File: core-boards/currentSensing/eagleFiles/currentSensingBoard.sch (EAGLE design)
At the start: 22 parts, among them Q1 16MHz, X2 2-PIN_2MM-H, X3 4-PIN_2MM-H

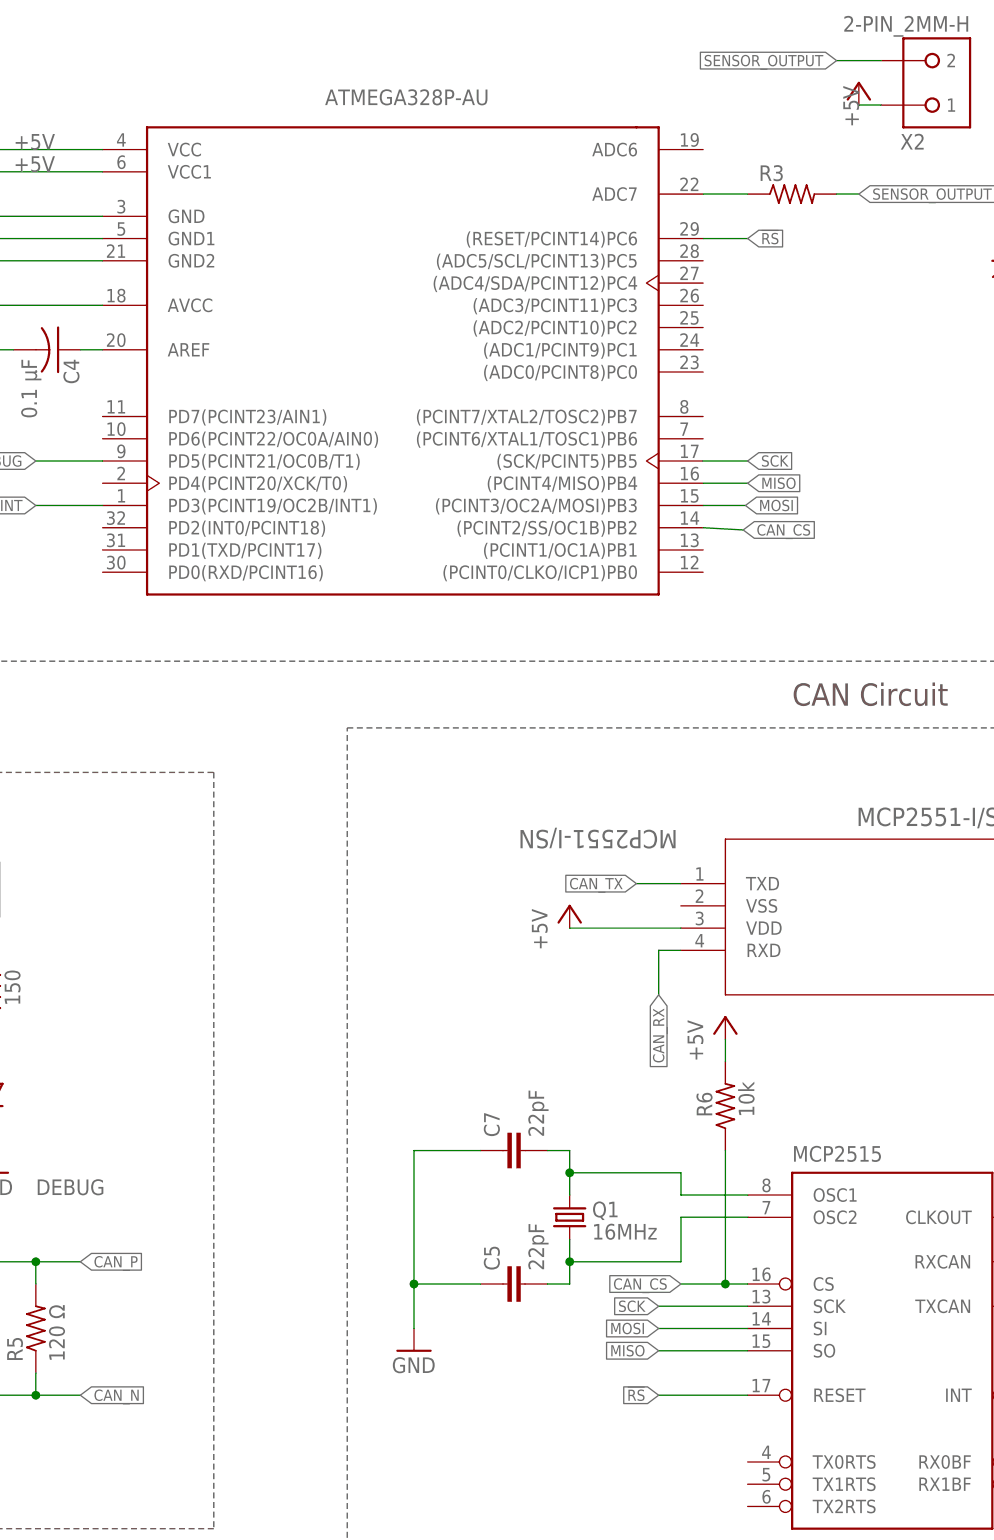
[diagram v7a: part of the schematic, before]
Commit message: Updated Oscillator
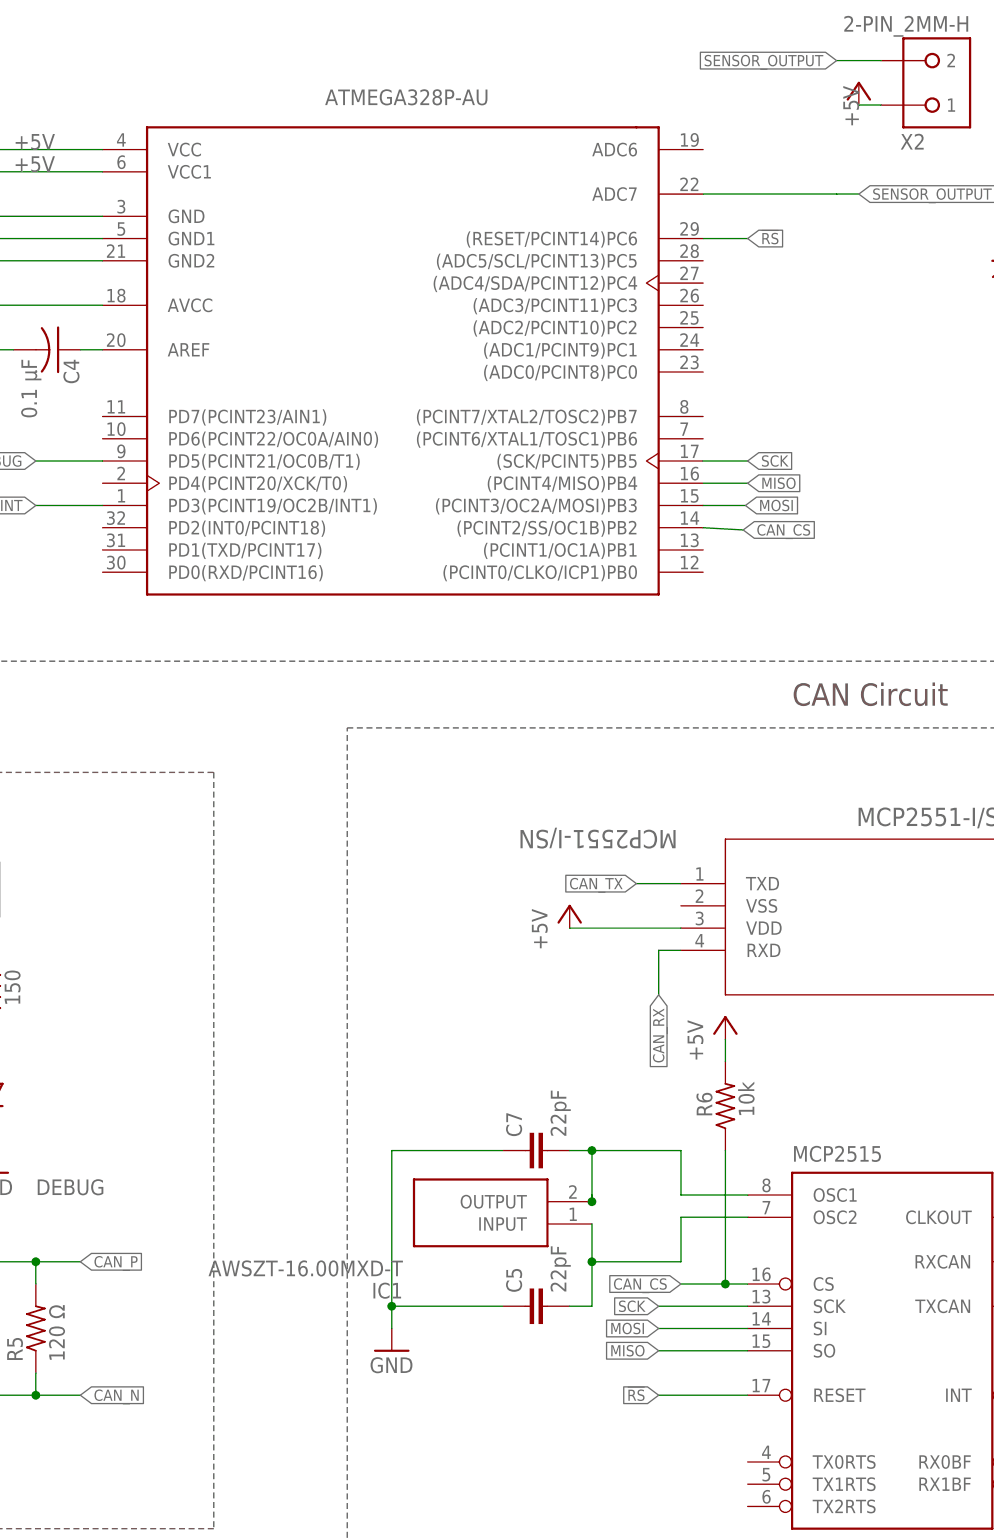
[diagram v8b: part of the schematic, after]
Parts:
- removed Q1: 16MHz, SparkFun-FreqCtrl:CRYSTAL5X3
- removed R3: (no value), RoboJackets-Resistors:R0603W
- added IC1: AWSZT-16.00MXD-T, AWSZT-16.00MXD-T:AWSZT-16.00MXD-T
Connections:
- removed net N$17: C7.2, MCP2515>NAME.OSC1, Q1.2
- removed net N$18: C5.2, MCP2515>NAME.OSC2, Q1.1
- removed net N$2: ATMEGA328P-AU(V1).ADC7, R3.PIN1
- new net CLK1: C5.2, IC1.INPUT, MCP2515>NAME.OSC2
- new net CLK2: C7.2, IC1.OUTPUT, MCP2515>NAME.OSC1
- net SENSOR_OUTPUT: now also ATMEGA328P-AU(V1).ADC7; no longer R3.PIN2
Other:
- moved on the sheet: C5, C7
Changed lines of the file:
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@@
 <?xml version="1.0" encoding="utf-8"?>
 <!DOCTYPE eagle SYSTEM "eagle.dtd">
-<eagle version="9.5.2">
+<eagle version="9.6.2">
 <drawing>
 <settings>
@@
 <part name="C6" library="rcl" library_urn="urn:adsk.eagle:library:334" deviceset="C-US" device="C0603" package3d_urn="urn:adsk.eagle:package:23616/2" value="0.1 µF"/>
 <part name="MCP2515" library="SparkFun-DigitalIC" deviceset="MCP2510" device="SO" value="MCP2515"/>
-<part name="Q1" library="SparkFun-FreqCtrl" deviceset="CRYSTAL" device="5X3" value="16MHz"/>
 <part name="C5" library="SparkFun-Capacitors" deviceset="22PF-50V-5%(0603)" device="" value="22pF"/>
 <part name="C7" library="SparkFun-Capacitors" deviceset="22PF-50V-5%(0603)" device="" value="22pF"/>
@@
 <part name="DEBUG" library="RoboJackets-LEDs" deviceset="LED-SMD" device="" technology="-RED" value="RED"/>
 <part name="FRAME1" library="RoboJackets-Frames" deviceset="FRAME_B_L" device=""/>
-<part name="R3" library="RoboJackets-Resistors" deviceset="R0603W" device=""/>
+<part name="IC1" library="AWSZT-16.00MXD-T" deviceset="AWSZT-16.00MXD-T" device=""/>
 </parts>
 <sheets>
@@
 <attribute name="VALUE" x="200.66" y="49.53" size="1.778" layer="96"/>
 </instance>
-<instance part="Q1" gate="G$1" x="175.26" y="88.9" smashed="yes" rot="R90">
-<attribute name="NAME" x="177.8" y="88.9" size="1.778" layer="95"/>
-<attribute name="VALUE" x="177.8" y="86.36" size="1.778" layer="96"/>
-</instance>
-<instance part="C5" gate="G$1" x="170.18" y="81.28" smashed="yes" rot="R90">
-<attribute name="NAME" x="167.259" y="82.804" size="1.778" layer="95" rot="R90"/>
-<attribute name="VALUE" x="172.339" y="82.804" size="1.778" layer="96" rot="R90"/>
-</instance>
-<instance part="C7" gate="G$1" x="170.18" y="96.52" smashed="yes" rot="R90">
-<attribute name="NAME" x="167.259" y="98.044" size="1.778" layer="95" rot="R90"/>
-<attribute name="VALUE" x="172.339" y="98.044" size="1.778" layer="96" rot="R90"/>
-</instance>
-<instance part="GND12" gate="1" x="157.48" y="73.66" smashed="yes">
-<attribute name="VALUE" x="154.94" y="71.12" size="1.778" layer="96"/>
+<instance part="C5" gate="G$1" x="172.72" y="78.74" smashed="yes" rot="R90">
+<attribute name="NAME" x="169.799" y="80.264" size="1.778" layer="95" rot="R90"/>
+<attribute name="VALUE" x="174.879" y="80.264" size="1.778" layer="96" rot="R90"/>
+</instance>
+<instance part="C7" gate="G$1" x="172.72" y="96.52" smashed="yes" rot="R90">
+<attribute name="NAME" x="169.799" y="98.044" size="1.778" layer="95" rot="R90"/>
+<attribute name="VALUE" x="174.879" y="98.044" size="1.778" layer="96" rot="R90"/>
+</instance>
+<instance part="GND12" gate="1" x="154.94" y="73.66" smashed="yes">
+<attribute name="VALUE" x="152.4" y="71.12" size="1.778" layer="96"/>
 </instance>
 <instance part="ICSP" gate="-1" x="317.5" y="137.16" smashed="yes">
@@
 <attribute name="SCH_DESC" x="326.39" y="6.35" size="2.54" layer="94"/>
 </instance>
-<instance part="R3" gate="G$1" x="200.66" y="205.74" smashed="yes">
-<attribute name="NAME" x="196.85" y="207.2386" size="1.778" layer="95"/>
-<attribute name="VALUE" x="196.85" y="202.438" size="1.778" layer="96"/>
+<instance part="IC1" gate="G$1" x="177.8" y="88.138" smashed="yes" rot="R180">
+<attribute name="NAME" x="156.21" y="80.518" size="1.778" layer="95" rot="R180" align="center-left"/>
+<attribute name="VALUE" x="156.21" y="83.058" size="1.778" layer="96" rot="R180" align="center-left"/>
 </instance>
 </instances>
@@
 </segment>
 <segment>
-<wire x1="165.1" y1="96.52" x2="157.48" y2="96.52" width="0.1524" layer="91"/>
-<wire x1="157.48" y1="96.52" x2="157.48" y2="81.28" width="0.1524" layer="91"/>
-<wire x1="157.48" y1="81.28" x2="165.1" y2="81.28" width="0.1524" layer="91"/>
-<wire x1="157.48" y1="76.2" x2="157.48" y2="81.28" width="0.1524" layer="91"/>
-<junction x="157.48" y="81.28"/>
-<pinref part="C7" gate="G$1" pin="1"/>
+<wire x1="154.94" y1="78.74" x2="167.64" y2="78.74" width="0.1524" layer="91"/>
+<wire x1="154.94" y1="76.2" x2="154.94" y2="78.74" width="0.1524" layer="91"/>
 <pinref part="C5" gate="G$1" pin="1"/>
 <pinref part="GND12" gate="1" pin="GND"/>
+<wire x1="154.94" y1="78.74" x2="154.94" y2="96.52" width="0.1524" layer="91"/>
+<junction x="154.94" y="78.74"/>
+<pinref part="C7" gate="G$1" pin="1"/>
+<wire x1="154.94" y1="96.52" x2="167.64" y2="96.52" width="0.1524" layer="91"/>
 </segment>
 <segment>
@@
 </segment>
 <segment>
-<pinref part="R3" gate="G$1" pin="PIN2"/>
 <wire x1="205.74" y1="205.74" x2="208.28" y2="205.74" width="0.1524" layer="91"/>
 <label x="208.28" y="205.74" size="1.27" layer="95" xref="yes"/>
-</segment>
-</net>
-<net name="N$17" class="0">
-<segment>
-<wire x1="175.26" y1="91.44" x2="175.26" y2="93.98" width="0.1524" layer="91"/>
-<wire x1="175.26" y1="93.98" x2="175.26" y2="96.52" width="0.1524" layer="91"/>
-<wire x1="172.72" y1="96.52" x2="175.26" y2="96.52" width="0.1524" layer="91"/>
-<wire x1="187.96" y1="93.98" x2="175.26" y2="93.98" width="0.1524" layer="91"/>
-<junction x="175.26" y="93.98"/>
-<pinref part="Q1" gate="G$1" pin="2"/>
+<pinref part="ATMEGA328P-AU(V1)" gate="G$1" pin="ADC7"/>
+<wire x1="190.5" y1="205.74" x2="205.74" y2="205.74" width="0.1524" layer="91"/>
+</segment>
+</net>
+<net name="CLK2" class="0">
+<segment>
+<wire x1="177.8" y1="91.44" x2="177.8" y2="90.678" width="0.1524" layer="91"/>
+<wire x1="177.8" y1="90.678" x2="177.8" y2="96.52" width="0.1524" layer="91"/>
+<wire x1="175.26" y1="96.52" x2="177.8" y2="96.52" width="0.1524" layer="91"/>
+<wire x1="187.96" y1="96.52" x2="177.8" y2="96.52" width="0.1524" layer="91"/>
+<junction x="177.8" y="96.52"/>
 <pinref part="C7" gate="G$1" pin="2"/>
-<wire x1="187.96" y1="91.44" x2="187.96" y2="93.98" width="0.1524" layer="91"/>
+<wire x1="187.96" y1="91.44" x2="187.96" y2="96.52" width="0.1524" layer="91"/>
 <pinref part="MCP2515" gate="&gt;NAME" pin="OSC1"/>
 <wire x1="187.96" y1="91.44" x2="195.58" y2="91.44" width="0.1524" layer="91"/>
-</segment>
-</net>
-<net name="N$18" class="0">
-<segment>
-<wire x1="175.26" y1="86.36" x2="175.26" y2="83.82" width="0.1524" layer="91"/>
-<wire x1="175.26" y1="83.82" x2="175.26" y2="81.28" width="0.1524" layer="91"/>
-<wire x1="172.72" y1="81.28" x2="175.26" y2="81.28" width="0.1524" layer="91"/>
-<wire x1="187.96" y1="83.82" x2="175.26" y2="83.82" width="0.1524" layer="91"/>
-<junction x="175.26" y="83.82"/>
-<pinref part="Q1" gate="G$1" pin="1"/>
+<pinref part="IC1" gate="G$1" pin="OUTPUT"/>
+<junction x="177.8" y="90.678"/>
+</segment>
+</net>
+<net name="CLK1" class="0">
+<segment>
+<wire x1="177.8" y1="83.82" x2="177.8" y2="78.74" width="0.1524" layer="91"/>
+<wire x1="175.26" y1="78.74" x2="177.8" y2="78.74" width="0.1524" layer="91"/>
+<wire x1="187.96" y1="83.82" x2="177.8" y2="83.82" width="0.1524" layer="91"/>
 <pinref part="C5" gate="G$1" pin="2"/>
 <pinref part="MCP2515" gate="&gt;NAME" pin="OSC2"/>
 <wire x1="187.96" y1="83.82" x2="187.96" y2="88.9" width="0.1524" layer="91"/>
 <wire x1="187.96" y1="88.9" x2="195.58" y2="88.9" width="0.1524" layer="91"/>
+<pinref part="IC1" gate="G$1" pin="INPUT"/>
+<wire x1="177.8" y1="88.138" x2="177.8" y2="83.82" width="0.1524" layer="91"/>
+<junction x="177.8" y="83.82"/>
 </segment>
 </net>
@@
 </segment>
 </net>
-<net name="N$2" class="0">
-<segment>
-<pinref part="ATMEGA328P-AU(V1)" gate="G$1" pin="ADC7"/>
-<pinref part="R3" gate="G$1" pin="PIN1"/>
-<wire x1="190.5" y1="205.74" x2="195.58" y2="205.74" width="0.1524" layer="91"/>
-</segment>
-</net>
